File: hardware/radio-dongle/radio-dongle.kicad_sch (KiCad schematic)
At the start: 29 parts, among them J1 USB_C_Receptacle, J2 Conn_01x15, J3 AVR-JTAG-10, SW1 SW_Push, U1 SN65HVD230, U2 STM32F103C8T6, Y1 12mhz

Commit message: i can't believe what they did to my boy
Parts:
- removed C10, C3, C4, C5, C6, C7: 100nf, Capacitor_SMD:C_0402_1005Metric, symbol Device:C_Small
- removed C2: 4.7nf, Capacitor_SMD:C_0805_2012Metric, symbol Device:C_Small
- removed C8, C9: C_Small, Capacitor_SMD:C_0402_1005Metric, symbol Device:C_Small
- removed D1: GRN, LED_SMD:LED_0603_1608Metric, symbol Device:D_Small
- removed D2: RED, LED_SMD:LED_0603_1608Metric, symbol Device:D_Small
- removed J3: AVR-JTAG-10, Connector_PinHeader_1.27mm:PinHeader_2x06_P1.27mm_Vertical_SMD, symbol Connector:AVR-JTAG-10
- removed JP1, JP2: Jumper_3_Open, Jumper:SolderJumper-3_P1.3mm_Open_Pad1.0x1.5mm_NumberLabels, symbol Jumper:Jumper_3_Open
- removed R2, R4: 240R, Resistor_SMD:R_0603_1608Metric, symbol Device:R_Small
- removed R3: 10k, Resistor_SMD:R_0402_1005Metric, symbol Device:R_Small
- removed R5, R6: 100k, Resistor_SMD:R_0402_1005Metric, symbol Device:R_Small
- removed SW1: SW_Push, ConeCodes:SW_RS-032G05A3-SMRT, symbol Switch:SW_Push
- removed U2: STM32F103C8T6, Package_QFP:LQFP-48_7x7mm_P0.5mm, symbol MCU_ST_STM32F1:STM32F103C8Tx
- removed Y1: 12mhz, Crystal:Crystal_SMD_3225-4Pin_3.2x2.5mm, symbol Device:Crystal_GND24_Small
- added U?: MCP73831-5-OT, Package_TO_SOT_SMD:SOT-23-5, symbol Battery_Management:MCP73831-5-OT
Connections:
- no-connect marks 29 -> 1
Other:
- moved on the sheet: J2

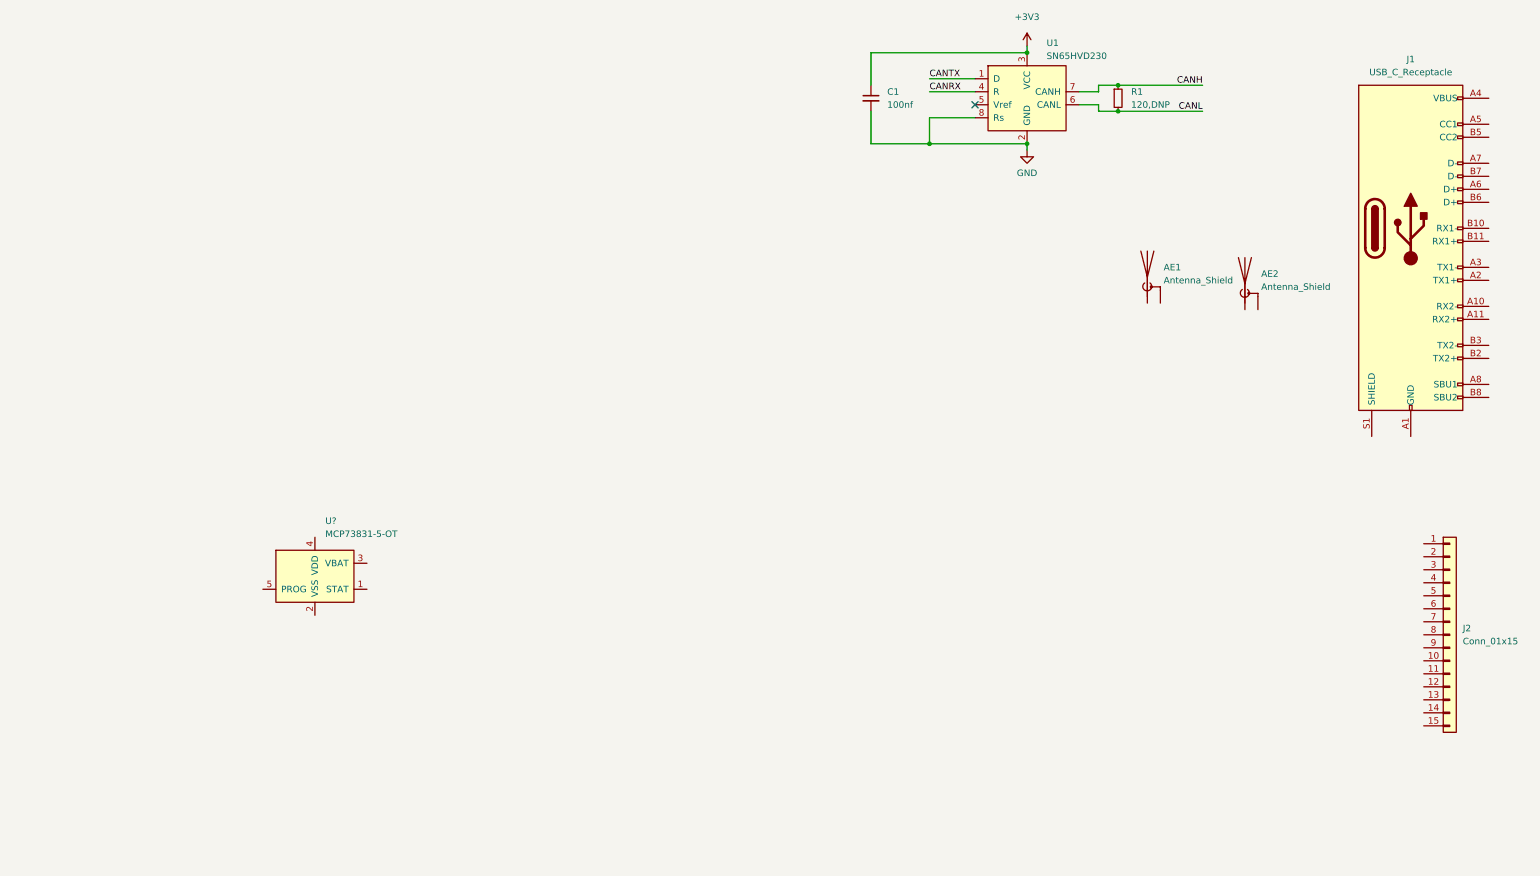
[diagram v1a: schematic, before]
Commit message: Hardware updates
* fix messed up +12v pin
* add a ground output for neopixels on both channels
* add a i2c microphone
* clean up schematic
* calculate component values for the LED drivers
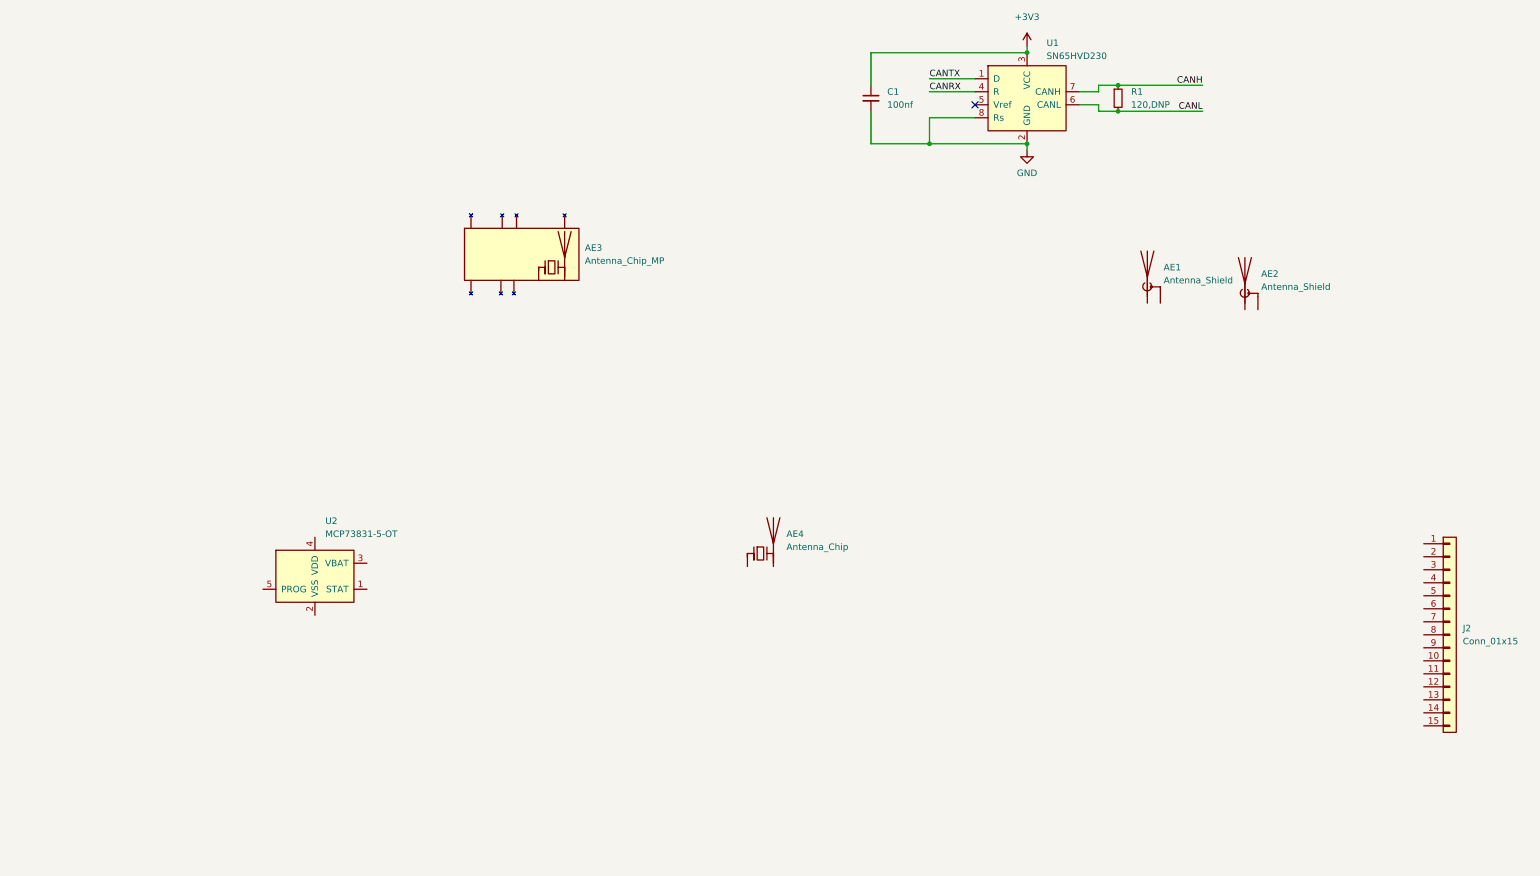
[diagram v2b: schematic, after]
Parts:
- removed J1: USB_C_Receptacle, Connector_USB:USB_C_Receptacle_HRO_TYPE-C-31-M-12, symbol Connector:USB_C_Receptacle
- added AE3: Antenna_Chip_MP, ConeCodes:SR4C033-L, symbol ConeCodes:Antenna_Chip_MP
- added AE4: Antenna_Chip, ConeCodes:SRCW004, symbol Device:Antenna_Chip
- gave numbers to parts that had none: 1
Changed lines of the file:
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@@
   (symbol (lib_id "Battery_Management:MCP73831-5-OT") (at 76.835 131.445 0) (unit 1)
     (in_bom yes) (on_board yes) (fields_autoplaced)
-    (property "Reference" "U?" (id 0) (at 78.8544 120.65 0)
+    (property "Reference" "U2" (id 0) (at 78.8544 120.65 0)
       (effects (font (size 1.27 1.27)) (justify left))
     )
@@
       (effects (font (size 1.27 1.27)) hide)
     )
+    (pin "1")
+    (pin "2")
+  )
+  (symbol (lib_id "ConeCodes:Antenna_Chip_MP") (at 132.715 73.66 0) (unit 1)
+    (in_bom yes) (on_board yes) (fields_autoplaced)
+    (property "Reference" "AE3" (id 0) (at 129.54 67.3099 0)
+      (effects (font (size 1.27 1.27)) (justify left))
+    )
+    (property "Value" "Antenna_Chip_MP" (id 1) (at 129.54 69.8499 0)
+      (effects (font (size 1.27 1.27)) (justify left))
+    )
+    (property "Footprint" "ConeCodes:SR4C033-L" (id 2) (at 120.523 66.675 0)
+      (effects (font (size 1.27 1.27)) hide)
+    )
+    (property "Datasheet" "~" (id 3) (at 120.523 66.675 0)
+      (effects (font (size 1.27 1.27)) hide)
+    )
+    (pin "3")
+    (pin "4")
+    (pin "5")
+    (pin "6")
+    (pin "7")
+    (pin "8")
+    (pin "9")
     (pin "1")
     (pin "2")
@@
     (pin "9")
   )
-  (symbol (lib_id "Connector:USB_C_Receptacle") (at 290.83 63.5 0) (unit 1)
-    (in_bom yes) (on_board yes) (fields_autoplaced)
-    (property "Reference" "J1" (id 0) (at 290.83 30.48 0))
-    (property "Value" "USB_C_Receptacle" (id 1) (at 290.83 33.02 0))
-    (property "Footprint" "Connector_USB:USB_C_Receptacle_HRO_TYPE-C-31-M-12" (id 2) (at 294.64 63.5 0)
-      (effects (font (size 1.27 1.27)) hide)
-    )
-    (property "Datasheet" "https://www.usb.org/sites/default/files/documents/usb_type-c.zip" (id 3) (at 294.64 63.5 0)
-      (effects (font (size 1.27 1.27)) hide)
-    )
-    (pin "A1")
-    (pin "A10")
-    (pin "A11")
-    (pin "A12")
-    (pin "A2")
-    (pin "A3")
-    (pin "A4")
-    (pin "A5")
-    (pin "A6")
-    (pin "A7")
-    (pin "A8")
-    (pin "A9")
-    (pin "B1")
-    (pin "B10")
-    (pin "B11")
-    (pin "B12")
-    (pin "B2")
-    (pin "B3")
-    (pin "B4")
-    (pin "B5")
-    (pin "B6")
-    (pin "B7")
-    (pin "B8")
-    (pin "B9")
-    (pin "S1")
+  (symbol (lib_id "Device:Antenna_Chip") (at 163.83 127 0) (unit 1)
+    (in_bom yes) (on_board yes) (fields_autoplaced)
+    (property "Reference" "AE4" (id 0) (at 168.91 123.1899 0)
+      (effects (font (size 1.27 1.27)) (justify left))
+    )
+    (property "Value" "Antenna_Chip" (id 1) (at 168.91 125.7299 0)
+      (effects (font (size 1.27 1.27)) (justify left))
+    )
+    (property "Footprint" "ConeCodes:SRCW004" (id 2) (at 161.29 122.555 0)
+      (effects (font (size 1.27 1.27)) hide)
+    )
+    (property "Datasheet" "~" (id 3) (at 161.29 122.555 0)
+      (effects (font (size 1.27 1.27)) hide)
+    )
+    (pin "1")
+    (pin "2")
   )
   (sheet_instances
@@
       (reference "AE2") (unit 1) (value "Antenna_Shield") (footprint "ConeCodes:60312202114509")
     )
+    (path "/6f2a454c-fde5-4ec4-ad12-a45eb97a1738"
+      (reference "AE3") (unit 1) (value "Antenna_Chip_MP") (footprint "ConeCodes:SR4C033-L")
+    )
+    (path "/d744173c-0915-4126-b1c0-6d25b2b79b70"
+      (reference "AE4") (unit 1) (value "Antenna_Chip") (footprint "ConeCodes:SRCW004")
+    )
     (path "/83d0f97d-5c34-4f18-8550-356716e2ac37"
       (reference "C1") (unit 1) (value "100nf") (footprint "Capacitor_SMD:C_0402_1005Metric")
     )
-    (path "/b000e08e-cd60-4333-a940-1ea0c4cbbf3c"
-      (reference "J1") (unit 1) (value "USB_C_Receptacle") (footprint "Connector_USB:USB_C_Receptacle_HRO_TYPE-C-31-M-12")
-    )
     (path "/afd0ccf3-aa21-4dc1-9153-ff6b5c3524c4"
       (reference "J2") (unit 1) (value "Conn_01x15") (footprint "Connector_FFC-FPC:Molex_502244-2430_1x24-1MP_P0.5mm_Horizontal")
@@
     )
     (path "/0ad6eefa-cb12-4c19-998c-2fb7e9721258"
-      (reference "U?") (unit 1) (value "MCP73831-5-OT") (footprint "Package_TO_SOT_SMD:SOT-23-5")
-    )
-  )
+      (reference "U2") (unit 1) (value "MCP73831-5-OT") (footprint "Package_TO_SOT_SMD:SOT-23-5")
+    )
+  )
